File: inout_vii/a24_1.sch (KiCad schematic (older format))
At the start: 19 parts, among them U23030 74HC04, U24001 74HC04, U24002 74HC04, U24003 74HC04, U24004 74HC02, U24005 74HC04, U24006 74HC27, U24007 74HC02, U24008 74HC04, U24009 74HC02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

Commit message: Lots of initial conditions, some missed gates, and some wiring fixes
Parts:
- U24033: Initial (none) -> 1
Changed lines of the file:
@@
 F 2 "" H 8300 7250 60  0000 C CNN
 F 3 "" H 8300 7250 60  0000 C CNN
+F 4 "1" H 8350 7250 60  0000 C CIN "Initial"
 	1    8300 7250
 	1    0    0    -1
@@
 F 2 "" H 8300 7750 60  0000 C CNN
 F 3 "" H 8300 7750 60  0000 C CNN
+F 4 "1" H 8350 7750 60  0000 C CIN "Initial"
 	2    8300 7750
 	1    0    0    -1
@@
 F 2 "" H 8300 8250 60  0000 C CNN
 F 3 "" H 8300 8250 60  0000 C CNN
+F 4 "1" H 8350 8250 60  0000 C CIN "Initial"
 	3    8300 8250
 	1    0    0    -1
@@
 F 2 "" H 8300 8750 60  0000 C CNN
 F 3 "" H 8300 8750 60  0000 C CNN
+F 4 "1" H 8350 8750 60  0000 C CIN "Initial"
 	4    8300 8750
 	1    0    0    -1

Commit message: Corrected some bad part identifiers
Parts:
- renumbered U23030 to U24030
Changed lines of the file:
@@
 	6600 4950 6550 4950
 $Comp
-L 74HC04 U23030
+L 74HC04 U24030
 U 2 1 5727F72D
 P 8300 4850
-F 0 "U23030" H 8450 4950 40  0000 C CNN
+F 0 "U24030" H 8450 4950 40  0000 C CNN
 F 1 "74HC04" H 8500 4750 40  0000 C CNN
 F 2 "" H 8300 4850 60  0000 C CNN

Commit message: Broke out some PIPA and CDU-related output signals, and fixed the polarity of PIPPLS/
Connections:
- net PIPPLS/: now also U24004.11, U24004.8, U24005.12, U24007.2; no longer U24005.13, U24006.12
- new net: U24005.13, U24006.12
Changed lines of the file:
@@
 	11150 1250 11300 1250
 Wire Wire Line
-	11200 1250 11200 1000
+	12250 1000 12250 2250
 Wire Wire Line
-	11200 1000 11350 1000
-Connection ~ 11200 1250
-Text HLabel 11350 1000 2    60   Output ~ 0
+	12250 1000 13600 1000
+Text HLabel 13600 1000 2    60   Output ~ 0
 PIPPLS/
 $Comp
@@
 $EndComp
 Wire Wire Line
-	12250 1250 12250 2250
-Wire Wire Line
 	12250 1750 12300 1750

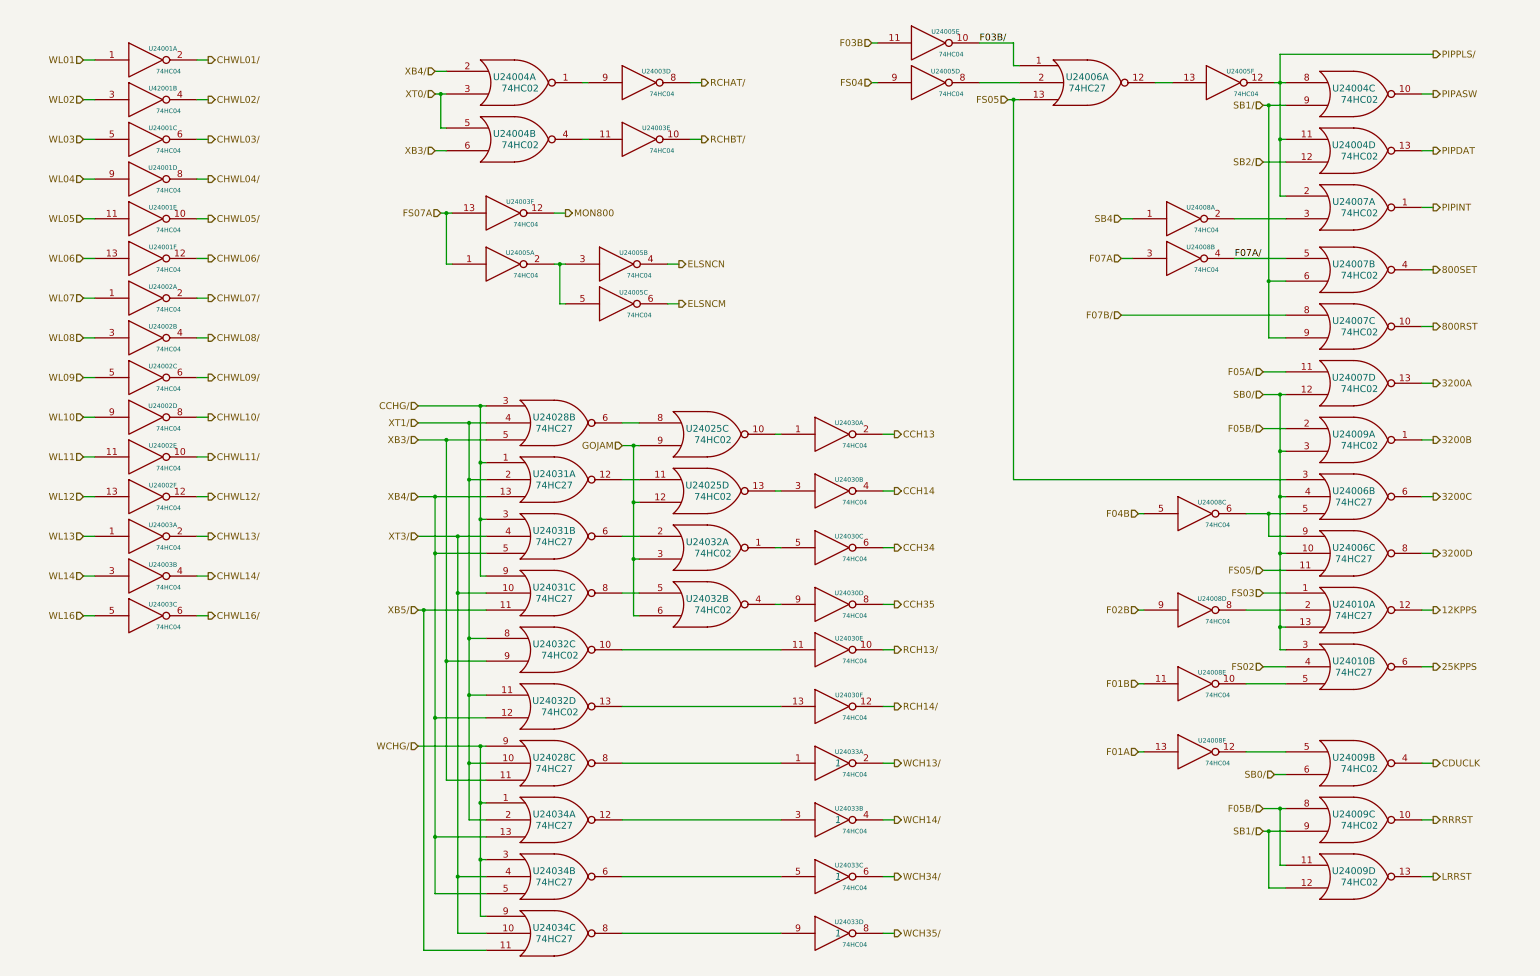
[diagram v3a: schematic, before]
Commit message: Fixed not->1-input nor in the rest of the modules.
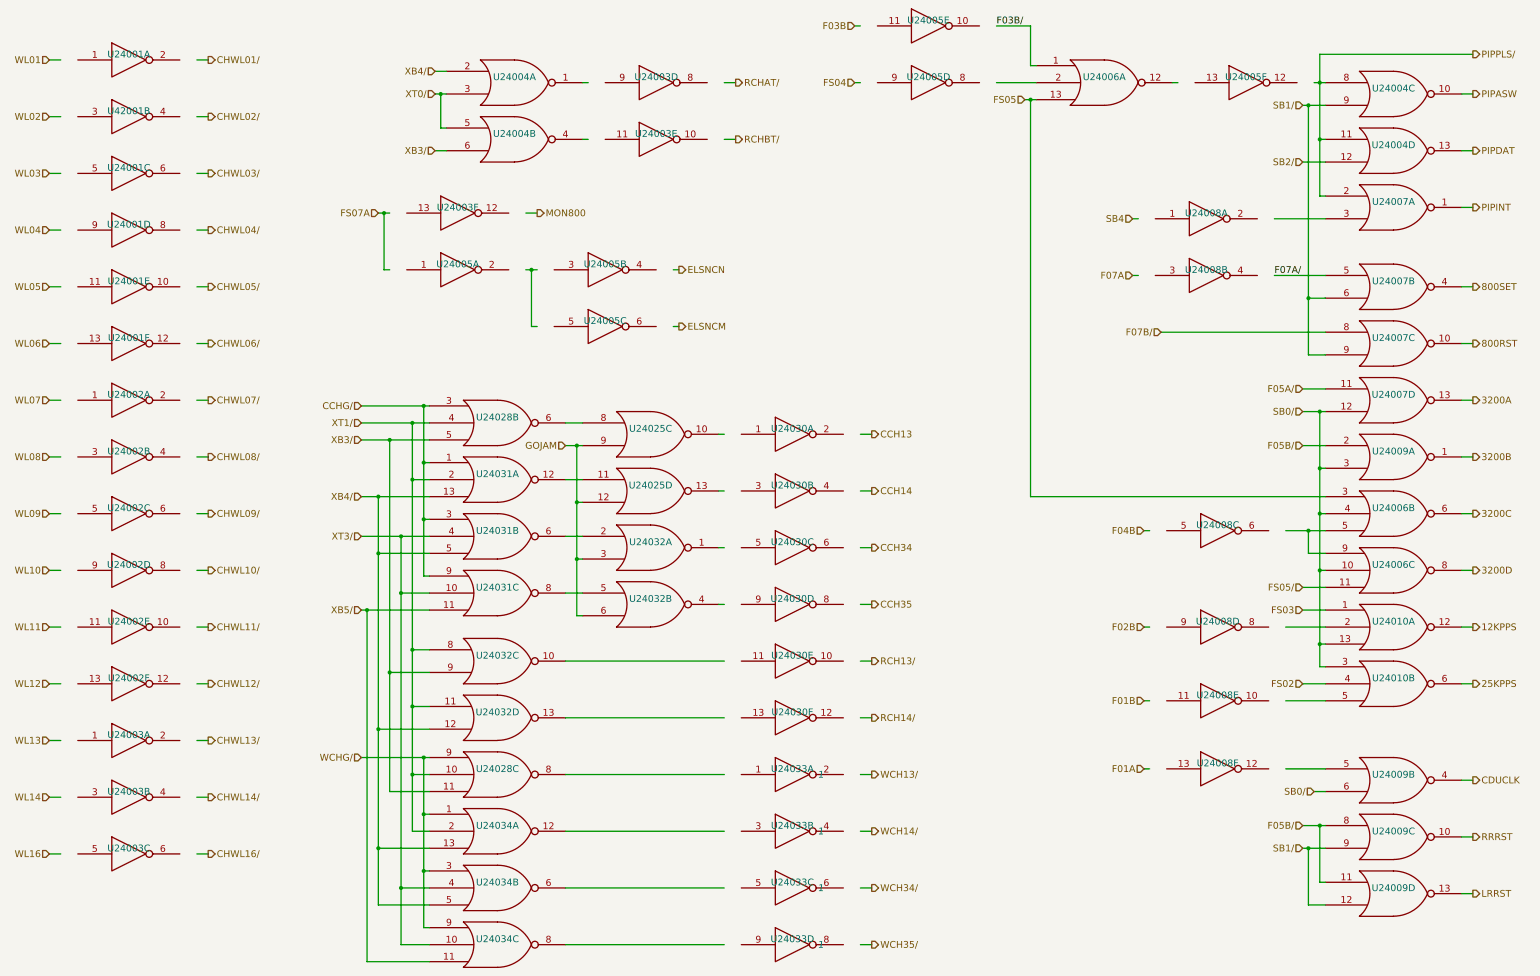
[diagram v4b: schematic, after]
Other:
- moved on the sheet: U24001A, U24001C, U24001D, U24001E, U24001F, U24002A, U24002B, U24002C, U24002D, U24002E, U24002F, U24003A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

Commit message: Added the CH77 alarm box (restart monitor) and switched most (all?) monitor outputs over to open drain, largely using new 74LVC06 parts (which are used *only* for monitor outputs)
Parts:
- removed unit 6 of U24003
- added U24038: 74LVC06, symbol 74LVC06
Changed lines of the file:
@@
 Wire Wire Line
 	7450 1750 7350 1750
-$Comp
-L 74HC04 U24003
-U 6 1 571CC56F
-P 5000 2400
-AR Path="/571CC56F" Ref="U24003"  Part="6"
-AR Path="/5714718A/571CC56F" Ref="U24003"  Part="6"
-F 0 "U24003" H 5000 2450 60  0000 C CNN
-F 1 "74HC04" H 5000 2150 60  0001 C CNN
-F 2 "" H 5000 2400 60  0000 C CNN
-F 3 "" H 5000 2400 60  0000 C CNN
-	6    5000 2400
-	1    0    0    -1
-$EndComp
 Wire Wire Line
 	4300 2400 4400 2400
@@
 	4350 2900 4400 2900
 Connection ~ 4350 2400
-Text HLabel 5700 2400 2    60   Output ~ 0
+Text HLabel 5400 2400 2    60   Output ~ 0
 MON800
 Wire Wire Line
-	5700 2400 5600 2400
+	5400 2400 5300 2400
 $Comp
 L 74HC04 U24005
@@
 	4200 9000 4750 9000
 Connection ~ 4200 5900
+$Comp
+L 74LVC06 U24038
+U 1 1 58958AC3
+P 4850 2400
+F 0 "U24038" H 5000 2550 60  0000 C CNN
+F 1 "74LVC06" H 5100 2300 60  0000 C CNN
+F 2 "" H 4850 2400 60  0000 C CNN
+F 3 "" H 4850 2400 60  0000 C CNN
+	1    4850 2400
+	1    0    0    -1
+$EndComp
 $EndSCHEMATC
